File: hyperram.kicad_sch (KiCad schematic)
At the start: 7 parts, among them U11 S27KL0641DABHI023

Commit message: Update PCB naming
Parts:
- C102: footprint data-center-dram-tester-footprints:0603-cap -> data-center-rdimm-ddr4-tester-footprints:0603-cap; symbol data-center-dram-tester:C_47u_0603 -> data-center-rdimm-ddr4-tester:C_47u_0603
- C103, C104, C105: footprint data-center-dram-tester-footprints:0402-cap -> data-center-rdimm-ddr4-tester-footprints:0402-cap; symbol data-center-dram-tester:C_100n_0402 -> data-center-rdimm-ddr4-tester:C_100n_0402
- R56, R61: footprint data-center-dram-tester-footprints:0402-res -> data-center-rdimm-ddr4-tester-footprints:0402-res; symbol data-center-dram-tester:R_10k_0402 -> data-center-rdimm-ddr4-tester:R_10k_0402
- U11: footprint data-center-dram-tester-footprints:FBGA-24 -> data-center-rdimm-ddr4-tester-footprints:FBGA-24; symbol data-center-dram-tester:S27KL0641DABHI023 -> data-center-rdimm-ddr4-tester:S27KL0641DABHI023
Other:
- title: Data Center DRAM Tester -> Data Center RDIMM DDR4 Tester
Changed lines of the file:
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@@
   (paper "A3")
   (title_block
-    (title "Data Center DRAM Tester")
+    (title "Data Center RDIMM DDR4 Tester")
     (date "2023-02-01")
     (rev "1.2.1")
@@
     )
   )
-  (symbol (lib_id "data-center-dram-tester:S27KL0641DABHI023") (at 196.215 150.495 0) (unit 1)
+  (symbol (lib_id "data-center-rdimm-ddr4-tester:S27KL0641DABHI023") (at 196.215 150.495 0) (unit 1)
     (in_bom yes) (on_board yes)
     (property "Reference" "U11" (id 0) (at 196.215 125.984 0))
     (property "Value" "S27KL0641DABHI023" (id 1) (at 196.215 128.2954 0))
-    (property "Footprint" "data-center-dram-tester-footprints:FBGA-24" (id 2) (at 184.785 178.435 0)
+    (property "Footprint" "data-center-rdimm-ddr4-tester-footprints:FBGA-24" (id 2) (at 184.785 178.435 0)
       (effects (font (size 1.27 1.27)) (justify left bottom) hide)
     )
@@
     (pin "B2")
   )
-  (symbol (lib_id "data-center-dram-tester:C_47u_0603") (at 220.345 131.445 0) (unit 1)
+  (symbol (lib_id "data-center-rdimm-ddr4-tester:C_47u_0603") (at 220.345 131.445 0) (unit 1)
     (in_bom yes) (on_board yes)
     (property "Reference" "C102" (id 0) (at 220.98 128.905 0)
@@
       (effects (font (size 1.524 1.524)) hide)
     )
-    (property "Footprint" "data-center-dram-tester-footprints:0603-cap" (id 2) (at 225.425 126.365 0)
+    (property "Footprint" "data-center-rdimm-ddr4-tester-footprints:0603-cap" (id 2) (at 225.425 126.365 0)
       (effects (font (size 1.524 1.524)) (justify left) hide)
     )
@@
     (pin "2")
   )
-  (symbol (lib_id "data-center-dram-tester:C_100n_0402") (at 236.22 131.445 0) (unit 1)
+  (symbol (lib_id "data-center-rdimm-ddr4-tester:C_100n_0402") (at 236.22 131.445 0) (unit 1)
     (in_bom yes) (on_board yes)
     (property "Reference" "C104" (id 0) (at 236.22 128.905 0)
@@
       (effects (font (size 1.524 1.524)) hide)
     )
-    (property "Footprint" "data-center-dram-tester-footprints:0402-cap" (id 2) (at 241.3 126.365 0)
+    (property "Footprint" "data-center-rdimm-ddr4-tester-footprints:0402-cap" (id 2) (at 241.3 126.365 0)
       (effects (font (size 1.524 1.524)) (justify left) hide)
     )
@@
     (pin "2")
   )
-  (symbol (lib_id "data-center-dram-tester:GND") (at 220.345 135.255 0) (unit 1)
+  (symbol (lib_id "data-center-rdimm-ddr4-tester:GND") (at 220.345 135.255 0) (unit 1)
     (in_bom yes) (on_board yes)
     (property "Reference" "#PWR0260" (id 0) (at 220.345 141.605 0)
@@
     (pin "1")
   )
-  (symbol (lib_id "data-center-dram-tester:R_10k_0402") (at 167.005 132.715 270) (unit 1)
+  (symbol (lib_id "data-center-rdimm-ddr4-tester:R_10k_0402") (at 167.005 132.715 270) (unit 1)
     (in_bom yes) (on_board yes) (fields_autoplaced)
     (property "Reference" "R56" (id 0) (at 165.227 131.8804 90)
@@
       (effects (font (size 1.524 1.524)) hide)
     )
-    (property "Footprint" "data-center-dram-tester-footprints:0402-res" (id 2) (at 172.085 137.795 0)
+    (property "Footprint" "data-center-rdimm-ddr4-tester-footprints:0402-res" (id 2) (at 172.085 137.795 0)
       (effects (font (size 1.524 1.524)) (justify left) hide)
     )
@@
     (pin "2")
   )
-  (symbol (lib_id "data-center-dram-tester:GND") (at 228.6 135.255 0) (unit 1)
+  (symbol (lib_id "data-center-rdimm-ddr4-tester:GND") (at 228.6 135.255 0) (unit 1)
     (in_bom yes) (on_board yes)
     (property "Reference" "#PWR0261" (id 0) (at 228.6 141.605 0)
@@
     (pin "1")
   )
-  (symbol (lib_id "data-center-dram-tester:GND") (at 236.22 135.255 0) (unit 1)
+  (symbol (lib_id "data-center-rdimm-ddr4-tester:GND") (at 236.22 135.255 0) (unit 1)
     (in_bom yes) (on_board yes)
     (property "Reference" "#PWR0262" (id 0) (at 236.22 141.605 0)
@@
     (pin "1")
   )
-  (symbol (lib_id "data-center-dram-tester:C_100n_0402") (at 228.6 131.445 0) (unit 1)
+  (symbol (lib_id "data-center-rdimm-ddr4-tester:C_100n_0402") (at 228.6 131.445 0) (unit 1)
     (in_bom yes) (on_board yes)
     (property "Reference" "C103" (id 0) (at 228.6 128.905 0)
@@
       (effects (font (size 1.524 1.524)) hide)
     )
-    (property "Footprint" "data-center-dram-tester-footprints:0402-cap" (id 2) (at 233.68 126.365 0)
+    (property "Footprint" "data-center-rdimm-ddr4-tester-footprints:0402-cap" (id 2) (at 233.68 126.365 0)
       (effects (font (size 1.524 1.524)) (justify left) hide)
     )
@@
     (pin "2")
   )
-  (symbol (lib_id "data-center-dram-tester:R_10k_0402") (at 170.18 132.715 270) (unit 1)
+  (symbol (lib_id "data-center-rdimm-ddr4-tester:R_10k_0402") (at 170.18 132.715 270) (unit 1)
     (in_bom yes) (on_board yes) (fields_autoplaced)
     (property "Reference" "R61" (id 0) (at 171.958 131.8804 90)
@@
       (effects (font (size 1.524 1.524)) hide)
     )
-    (property "Footprint" "data-center-dram-tester-footprints:0402-res" (id 2) (at 175.26 137.795 0)
+    (property "Footprint" "data-center-rdimm-ddr4-tester-footprints:0402-res" (id 2) (at 175.26 137.795 0)
       (effects (font (size 1.524 1.524)) (justify left) hide)
     )
@@
     (pin "2")
   )
-  (symbol (lib_id "data-center-dram-tester:GND") (at 173.355 172.085 0) (unit 1)
+  (symbol (lib_id "data-center-rdimm-ddr4-tester:GND") (at 173.355 172.085 0) (unit 1)
     (in_bom yes) (on_board yes)
     (property "Reference" "#PWR0263" (id 0) (at 173.355 178.435 0)
@@
     (pin "1")
   )
-  (symbol (lib_id "data-center-dram-tester:C_100n_0402") (at 243.84 131.445 0) (unit 1)
+  (symbol (lib_id "data-center-rdimm-ddr4-tester:C_100n_0402") (at 243.84 131.445 0) (unit 1)
     (in_bom yes) (on_board yes)
     (property "Reference" "C105" (id 0) (at 243.84 128.905 0)
@@
       (effects (font (size 1.524 1.524)) hide)
     )
-    (property "Footprint" "data-center-dram-tester-footprints:0402-cap" (id 2) (at 248.92 126.365 0)
+    (property "Footprint" "data-center-rdimm-ddr4-tester-footprints:0402-cap" (id 2) (at 248.92 126.365 0)
       (effects (font (size 1.524 1.524)) (justify left) hide)
     )
@@
     (pin "2")
   )
-  (symbol (lib_id "data-center-dram-tester:GND") (at 243.84 135.255 0) (unit 1)
+  (symbol (lib_id "data-center-rdimm-ddr4-tester:GND") (at 243.84 135.255 0) (unit 1)
     (in_bom yes) (on_board yes)
     (property "Reference" "#PWR0264" (id 0) (at 243.84 141.605 0)

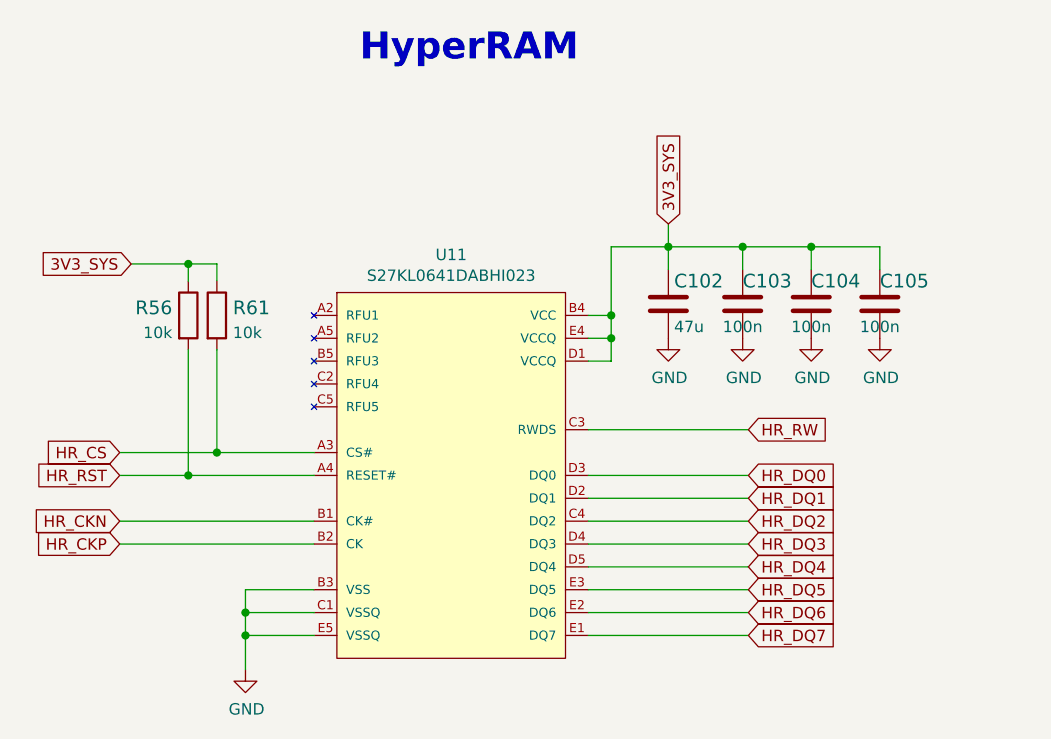
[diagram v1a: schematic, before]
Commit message: Introduce component standardization
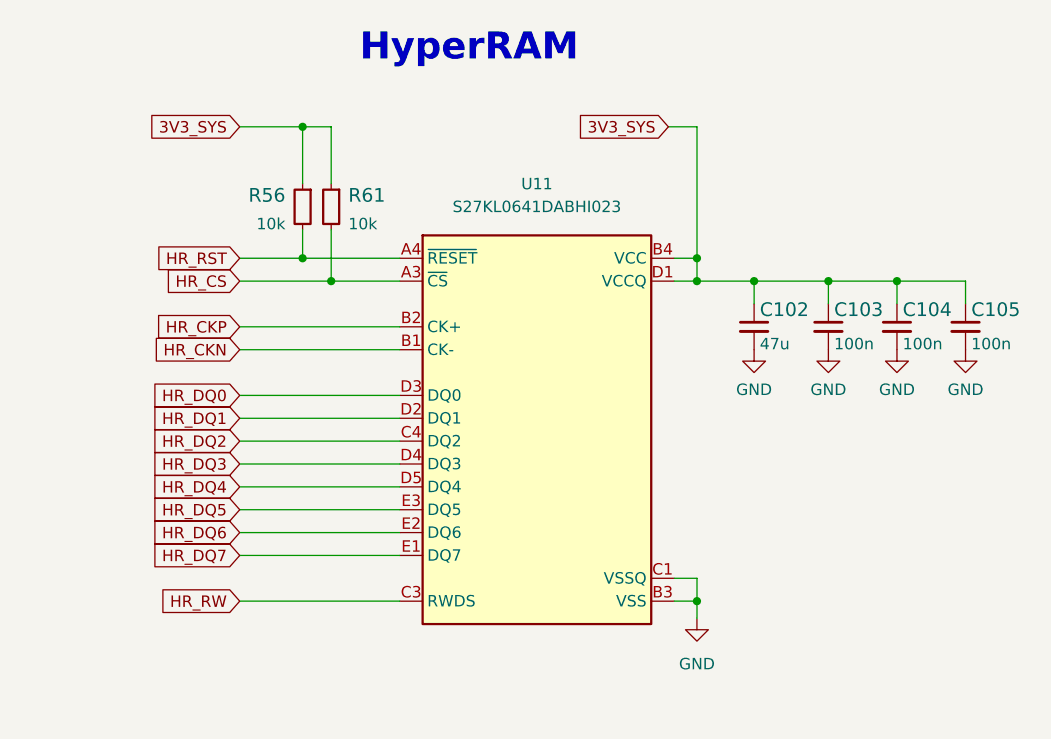
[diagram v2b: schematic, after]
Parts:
- C102: footprint data-center-rdimm-ddr4-tester-footprints:0603-cap -> data-center-rdimm-ddr4-tester-footprints:C_0603_1608Metric; Author (none) -> Antmicro; License (none) -> Apache-2.0; Manufacturer MURATA -> Murata
- C103, C104, C105: footprint data-center-rdimm-ddr4-tester-footprints:0402-cap -> data-center-rdimm-ddr4-tester-footprints:C_0402_1005Metric; Author (none) -> Antmicro; Dielectric (none) -> X5R; License (none) -> Apache-2.0; Voltage (none) -> 50V
- R56, R61: footprint data-center-rdimm-ddr4-tester-footprints:0402-res -> data-center-rdimm-ddr4-tester-footprints:R_0402_1005Metric; Author (none) -> Antmicro; License (none) -> Apache-2.0; MPN CRCW040210K0FKEDHP -> CR0402-FX-1002GLF; Manufacturer VISHAY -> Bourns; Tolerance (none) -> 1%
- U11: footprint data-center-rdimm-ddr4-tester-footprints:FBGA-24 -> data-center-rdimm-ddr4-tester-footprints:FBGA-24-1_6x8mm_Layout5x5_P1mm; Author (none) -> Antmicro; License (none) -> Apache-2.0; Manufacturer CYPRESS SEMICONDUCTOR -> Cypress Semiconductor
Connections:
- net at U11.A2 (NC): now also U11.A5 (NC), U11.B5 (NC), U11.C2 (NC), U11.C5 (NC)
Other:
- moved on the sheet: C102, C103, C104, C105, R56, R61

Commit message: [#55119] component update
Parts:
- C102: footprint data-center-rdimm-ddr4-tester-footprints:C_0603_1608Metric -> antmicro-footprints:C_0603_1608Metric; symbol data-center-rdimm-ddr4-tester:C_47u_0603 -> antmicroCapacitors0603:C_47u_0603
- C103, C104, C105: footprint data-center-rdimm-ddr4-tester-footprints:C_0402_1005Metric -> antmicro-footprints:C_0402_1005Metric; symbol data-center-rdimm-ddr4-tester:C_100n_0402 -> antmicroCapacitors0402:C_100n_0402
- R56, R61: footprint data-center-rdimm-ddr4-tester-footprints:R_0402_1005Metric -> antmicro-footprints:R_0402_1005Metric; symbol data-center-rdimm-ddr4-tester:R_10k_0402 -> antmicroResistors0402:R_10k_0402
- U11: footprint data-center-rdimm-ddr4-tester-footprints:FBGA-24-1_6x8mm_Layout5x5_P1mm -> antmicro-footprints:FBGA-25-24_6x8mm_Layout5x5_P1mm; symbol data-center-rdimm-ddr4-tester:S27KL0641DABHI023 -> antmicroMemory:S27KL0641DABHI023
